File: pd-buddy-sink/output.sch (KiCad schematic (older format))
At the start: 7 parts, among them J1 5-20 V⎓, Q1 MMBT2222ALT1G, Q2 DMP4015SSS

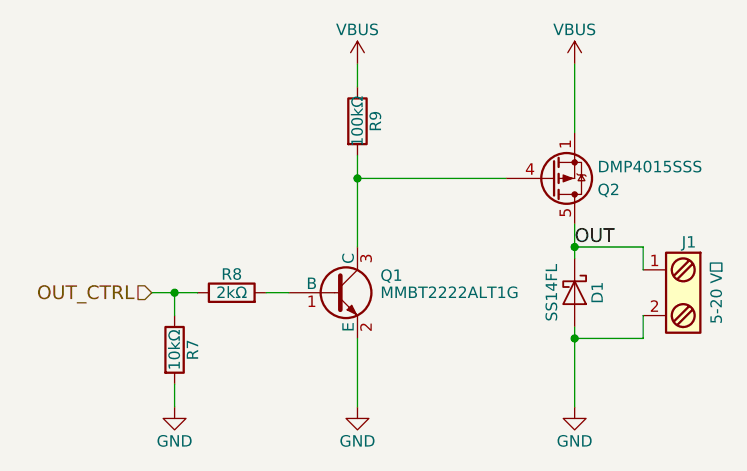
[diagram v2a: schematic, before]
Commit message: Changed Q1 to MMBT3904
It used to be an MMBT2222, now it's an MMBT3904.  The new transistor is
slightly lower-spec'd, but is still more than plenty for this
application.  Also, it's a MacroFab house part, so the boards will be
even cheaper to manufacture.
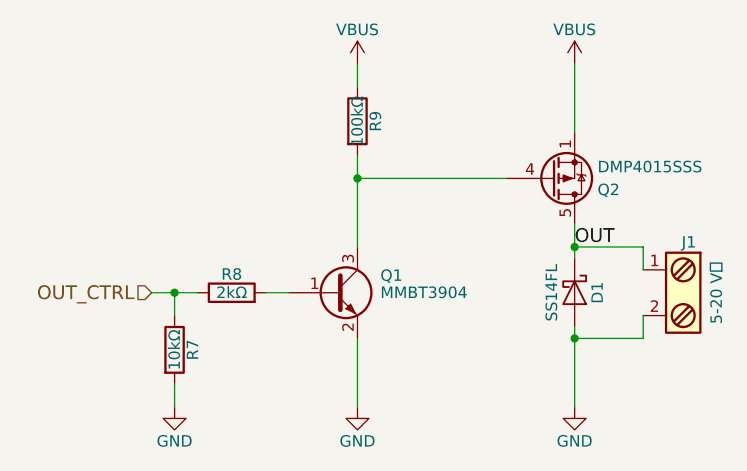
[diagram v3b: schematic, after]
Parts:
- removed Q1: MMBT2222ALT1G, TO_SOT_Packages_SMD:SOT-23, symbol MMBT2222AL
- added Q1: MMBT3904, TO_SOT_Packages_SMD:SOT-23, symbol MMBT3904
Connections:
- net GND: now also Q1.2 (E)
- net at Q2.4 (G), R9.2: now also Q1.3 (C)
- net at R8.2: now also Q1.1 (B)
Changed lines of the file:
@@
-$EndComp
-$Comp
-L MMBT2222AL Q1
-U 1 1 588FA577
-P 5450 4050
-F 0 "Q1" H 5650 4125 50  0000 L CNN
-F 1 "MMBT2222ALT1G" H 5650 4050 50  0000 L CNN
-F 2 "TO_SOT_Packages_SMD:SOT-23" H 5650 3975 50  0001 L CIN
-F 3 "" H 5450 4050 50  0000 L CNN
-	1    5450 4050
-	1    0    0    -1
 $EndComp
 $Comp
@@
 	1    0    0    -1
 $EndComp
+$Comp
+L MMBT3904 Q1
+U 1 1 59625136
+P 5450 4050
+F 0 "Q1" H 5650 4125 50  0000 L CNN
+F 1 "MMBT3904" H 5650 4050 50  0000 L CNN
+F 2 "TO_SOT_Packages_SMD:SOT-23" H 5650 3975 50  0001 L CIN
+F 3 "" H 5450 4050 50  0001 L CNN
+	1    5450 4050
+	1    0    0    -1
+$EndComp
